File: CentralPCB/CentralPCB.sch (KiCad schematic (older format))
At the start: 60 parts, among them J1 POWER HEADER, J2 SPI Header, J3 Conn_01x24, J4 Conn_01x24, J5 Conn_02x16_Odd_Even, J6 Conn_Coaxial, J7 Conn_02x10_Odd_Even, J8 Conn_01x05, U1 AD8531, U2 Teensy4.1, U3 BA7810CP-E2

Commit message: More routing CentralPCB
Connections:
- net +12V: no longer J8.4 (Pin_4)
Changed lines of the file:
@@
 	3100 7200 3550 7200
-Wire Wire Line
-	3550 7000 3100 7000
 Wire Wire Line
 	3100 7000 3100 7200
@@
 Wire Wire Line
 	3450 7100 3550 7100
-$Comp
-L power:+12V #PWR017
-U 1 1 6190D75E
-P 3350 6900
-F 0 "#PWR017" H 3350 6750 50  0001 C CNN
-F 1 "+12V" H 3365 7073 50  0000 C CNN
-F 2 "" H 3350 6900 50  0001 C CNN
-F 3 "" H 3350 6900 50  0001 C CNN
-	1    3350 6900
-	1    0    0    -1
-$EndComp
-Wire Wire Line
-	3350 6900 3350 7300
 Wire Wire Line
 	3350 7300 3550 7300
@@
 Wire Wire Line
 	850  1200 950  1200
+Wire Wire Line
+	3350 6900 3350 7300
+Wire Wire Line
+	3550 7000 3100 7000
+$Comp
+L power:+12V #PWR017
+U 1 1 6190D75E
+P 3350 6850
+F 0 "#PWR017" H 3350 6700 50  0001 C CNN
+F 1 "+12V" H 3365 7023 50  0000 C CNN
+F 2 "" H 3350 6850 50  0001 C CNN
+F 3 "" H 3350 6850 50  0001 C CNN
+	1    3350 6850
+	1    0    0    -1
+$EndComp
 $EndSCHEMATC

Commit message: Finished CentralPCB
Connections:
- net +12V: now also J8.4 (Pin_4)
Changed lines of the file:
@@
 	850  1200 950  1200
-Wire Wire Line
-	3350 6900 3350 7300
 Wire Wire Line
 	3550 7000 3100 7000
@@
 	1    0    0    -1
 $EndComp
+Wire Wire Line
+	3350 6850 3350 7300
 $EndSCHEMATC

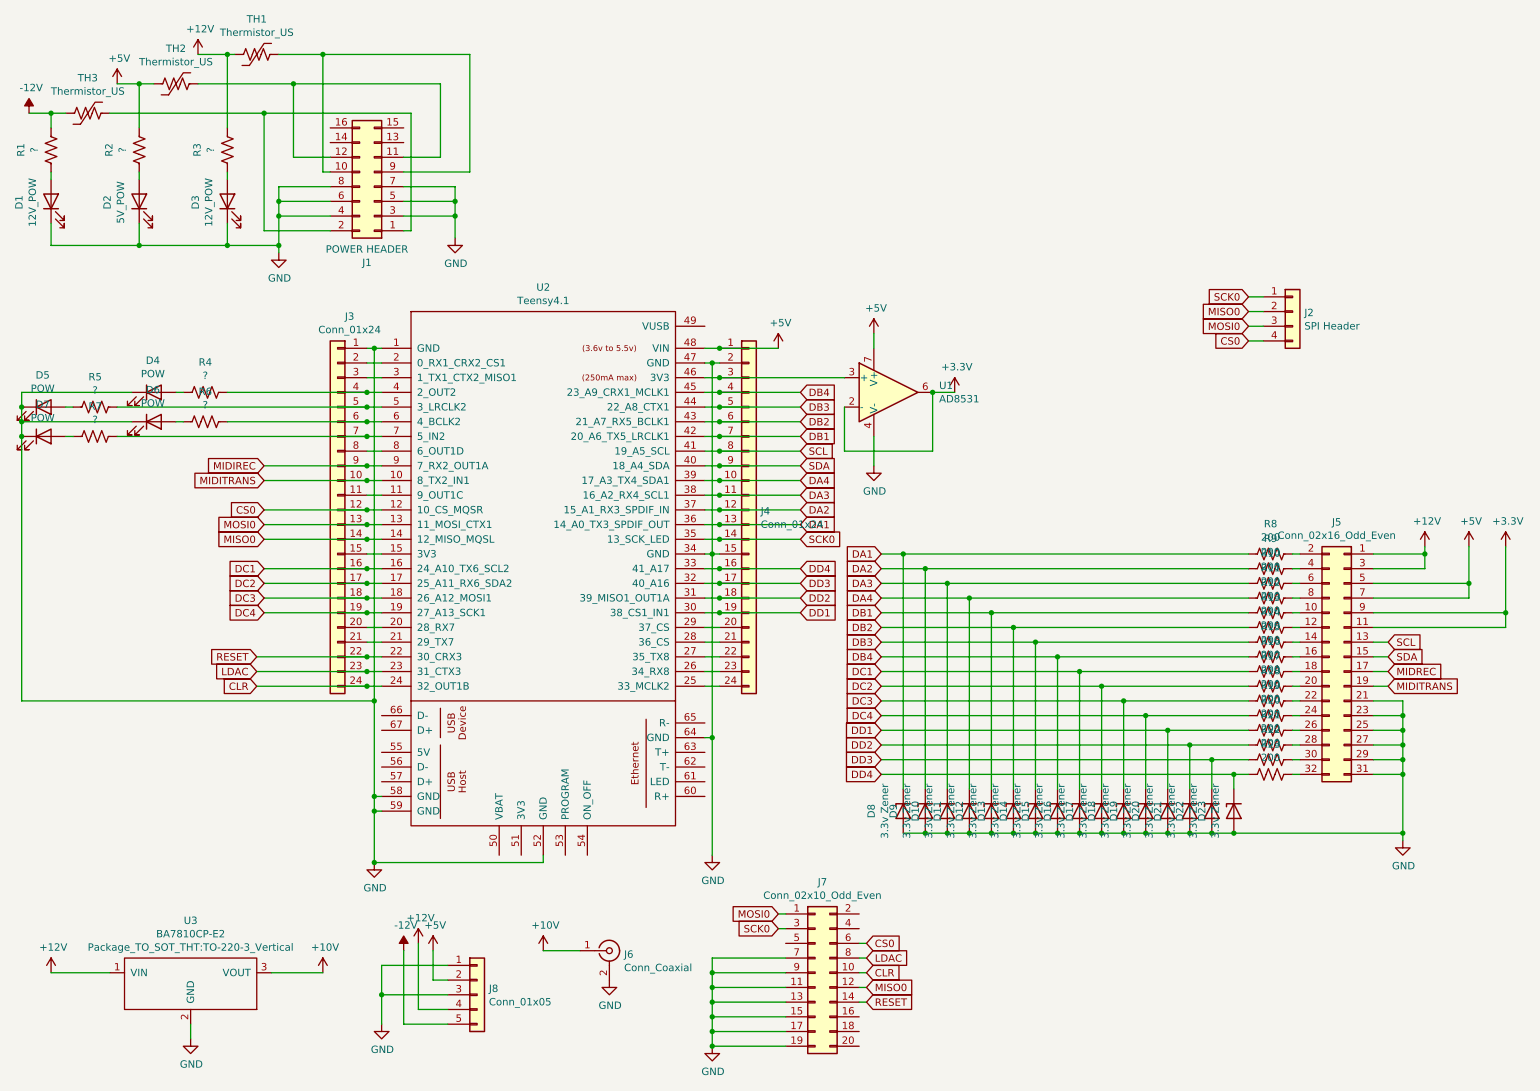
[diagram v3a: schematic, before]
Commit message: Added additional protection for CentralPCB
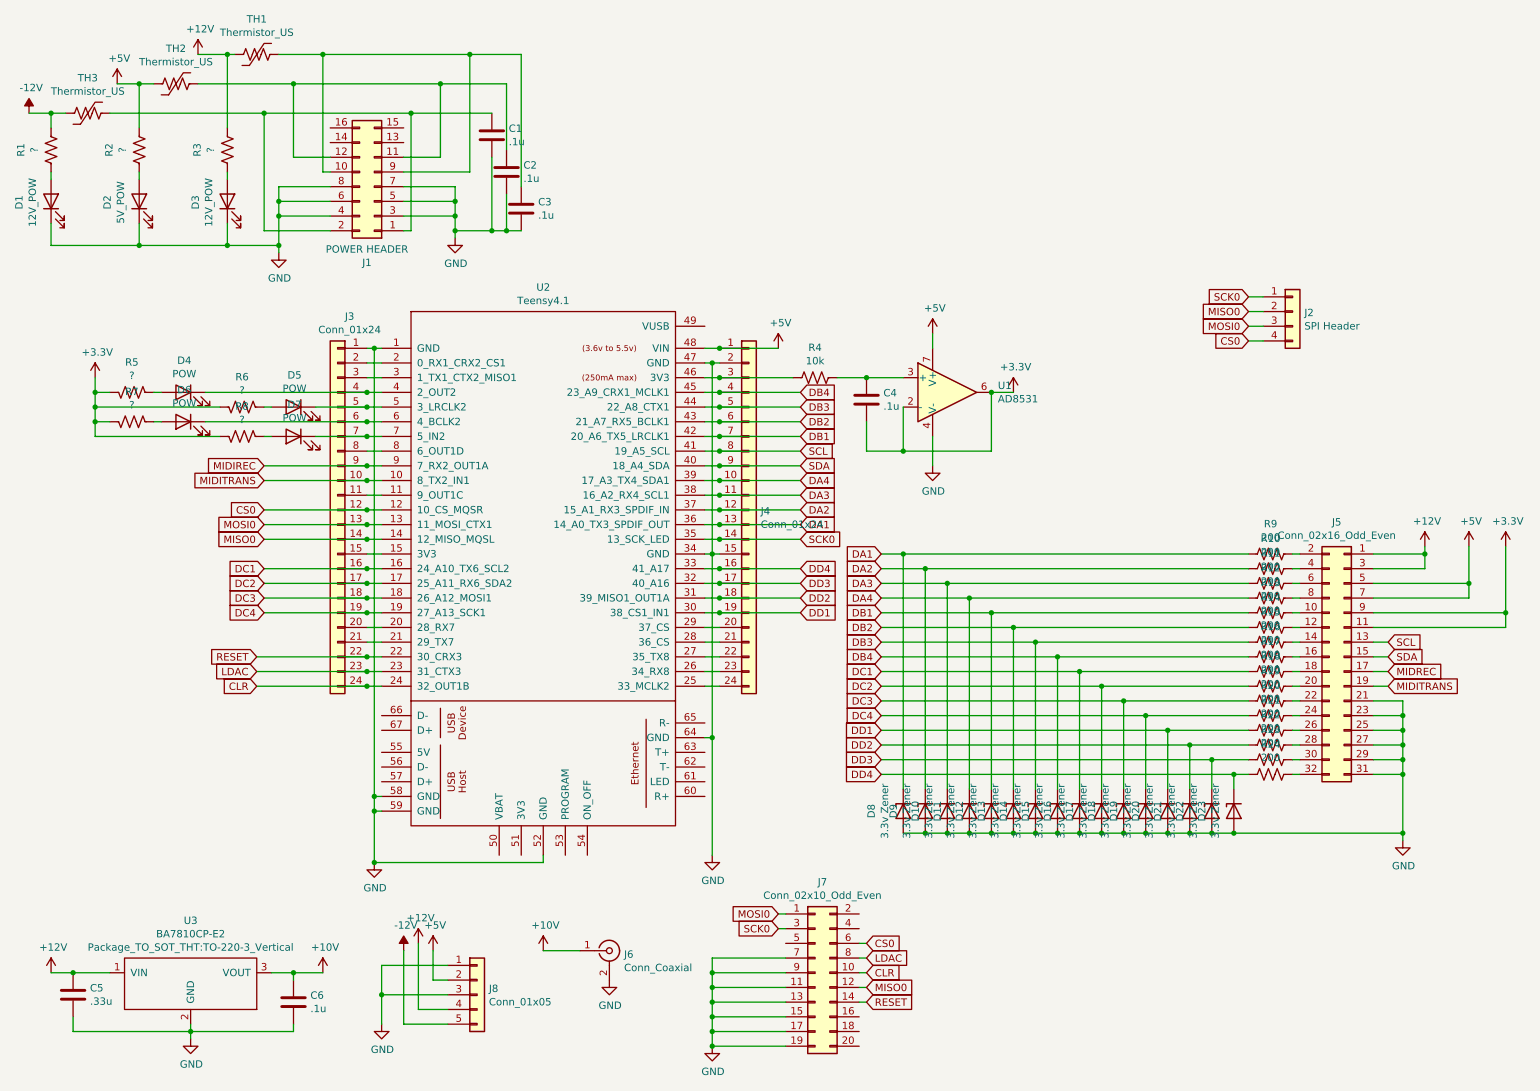
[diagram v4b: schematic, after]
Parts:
- added C1, C2, C3, C4, C6: .1u, Capacitor_SMD:C_0805_2012Metric, symbol Device:C
- added C5: .33u, Capacitor_SMD:C_0805_2012Metric, symbol Device:C
- added R4: 10k, Resistor_SMD:R_0805_2012Metric, symbol Device:R_US
- renumbered R9 to R10, R10 to R11, R11 to R12, R12 to R13, R13 to R14, R14 to R15, R15 to R16, R16 to R17, R17 to R18, R18 to R19, R19 to R20, R20 to R21, R21 to R22, R22 to R23, R23 to R24, R4 to R5, R5 to R6, R6 to R7, R7 to R8, R8 to R9
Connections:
- net +10V: now also C6.1
- net +12V: now also C5.1
- net +3V3: now also R5.1, R6.1, R7.1, R8.1, C4.2
- net GND: now also C1.2, C2.2, C3.2, C5.2, C6.2; no longer D4.1 (K), D5.1 (K), D6.1 (K), D7.1 (K)
- net at J1.1 (Pin_1), J1.2 (Pin_2), TH3.1: now also C1.1
- net at J1.10 (Pin_10), J1.9 (Pin_9), TH1.1: now also C3.1
- net at J1.11 (Pin_11), J1.12 (Pin_12), TH2.1: now also C2.1
- net at J3.4 (Pin_4), U2.4 (2_OUT2): now also D4.1 (K); no longer R5.1
- net at J3.5 (Pin_5), U2.5 (3_LRCLK2): now also D5.1 (K); no longer R6.1
- net at J3.6 (Pin_6), U2.6 (4_BCLK2): now also D6.1 (K); no longer R7.1
- net at J3.7 (Pin_7), U2.7 (5_IN2): now also D7.1 (K); no longer R8.1
- net at J4.3 (Pin_3), U2.46 (3V3): now also R4.2; no longer U1.3 (+)
- new net: C4.1, R4.1, U1.3 (+)
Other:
- moved on the sheet: D4, D5, D6, D7, R5, R6, R7, R8, U1
